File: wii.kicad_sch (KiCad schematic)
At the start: 7 parts, among them J1 12401598E4#2A, J2 54102-0164, U2 AZ1117-3.3

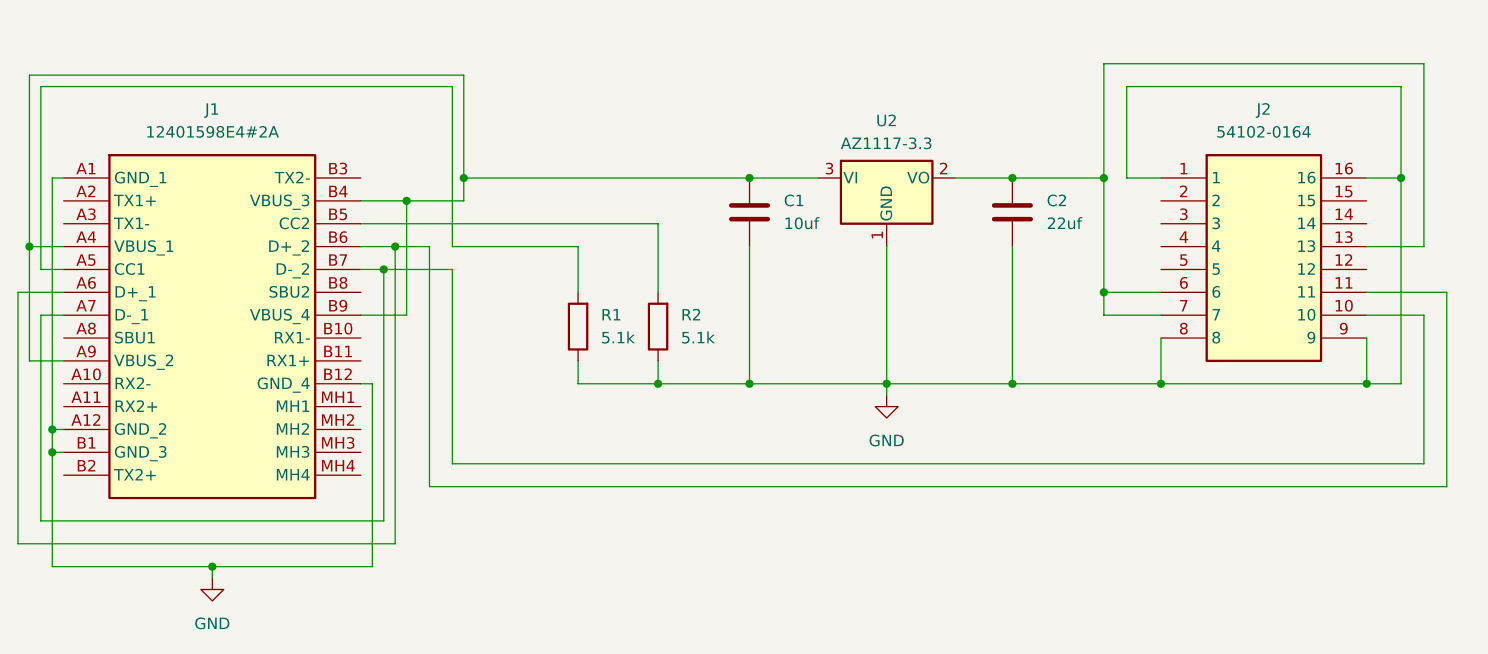
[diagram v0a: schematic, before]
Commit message: change to usb b
also added html bom plugin and removed round tracks
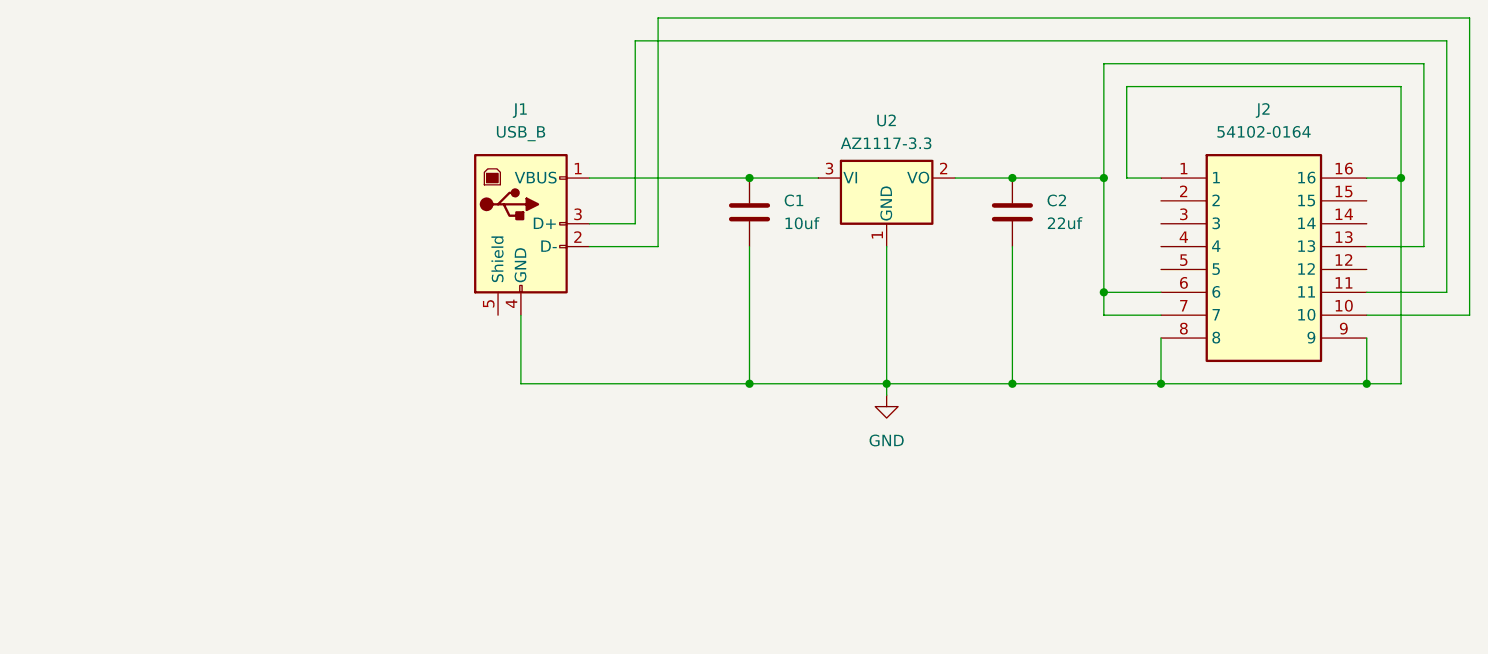
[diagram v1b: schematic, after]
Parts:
- removed J1: 12401598E4#2A, 12401598E42A, symbol SamacSys_Parts:12401598E4#2A
- removed R1, R2: 5.1k, Resistor_SMD:R_1206_3216Metric, symbol Device:R
- added J1: USB_B, Connector_USB:USB_B_OST_USB-B1HSxx_Horizontal, symbol Connector:USB_B
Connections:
- net GND: now also J1.4 (GND)
- net at C1.1, U2.3 (VI): now also J1.1 (VBUS)
- net at J2.11: now also J1.3 (D+)
- net at J2.10: now also J1.2 (D-)
